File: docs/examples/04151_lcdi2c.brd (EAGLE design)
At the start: 70.6 x 33.5 mm, 14 parts, among them IC1 PCF8574T, IC2 78L05Z

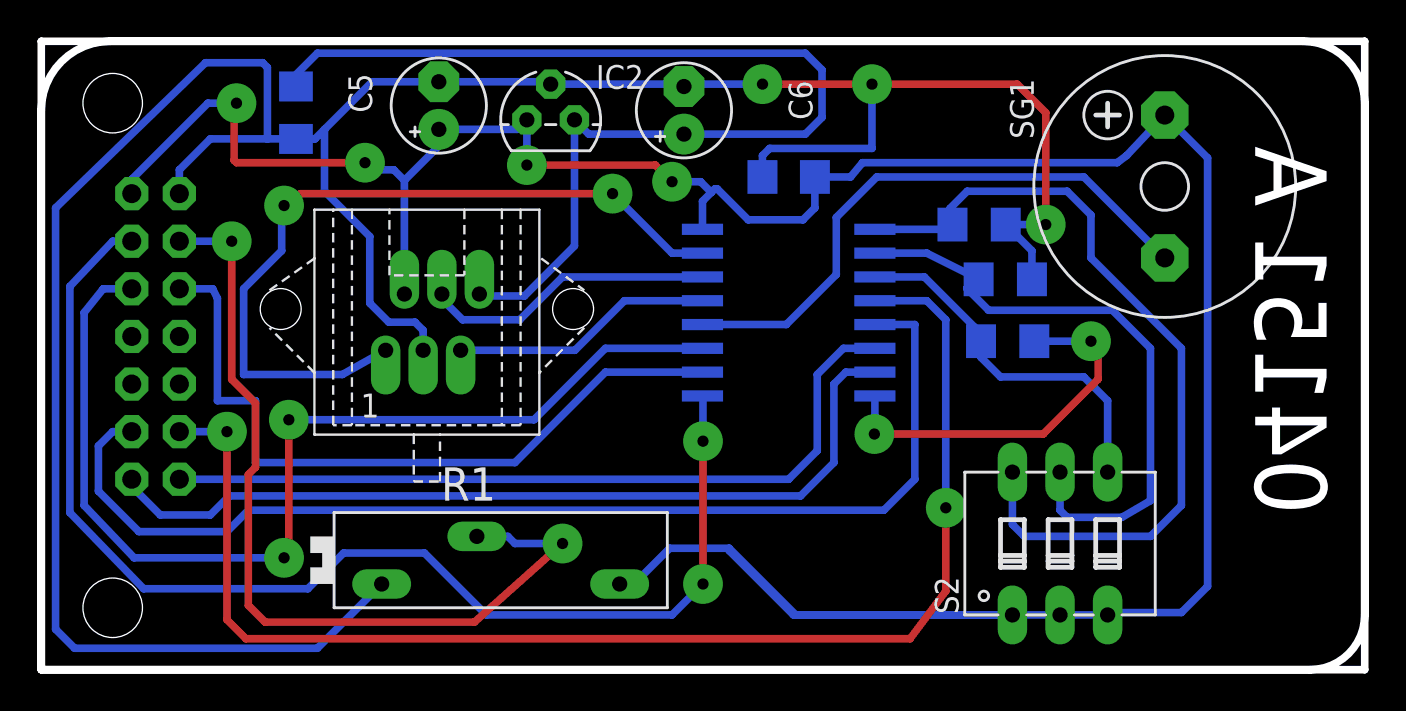
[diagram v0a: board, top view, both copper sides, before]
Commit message: Example 04151_lcdi2c.brd now include an arc at the origin, just for completeness of testing. Also updated camotics files.
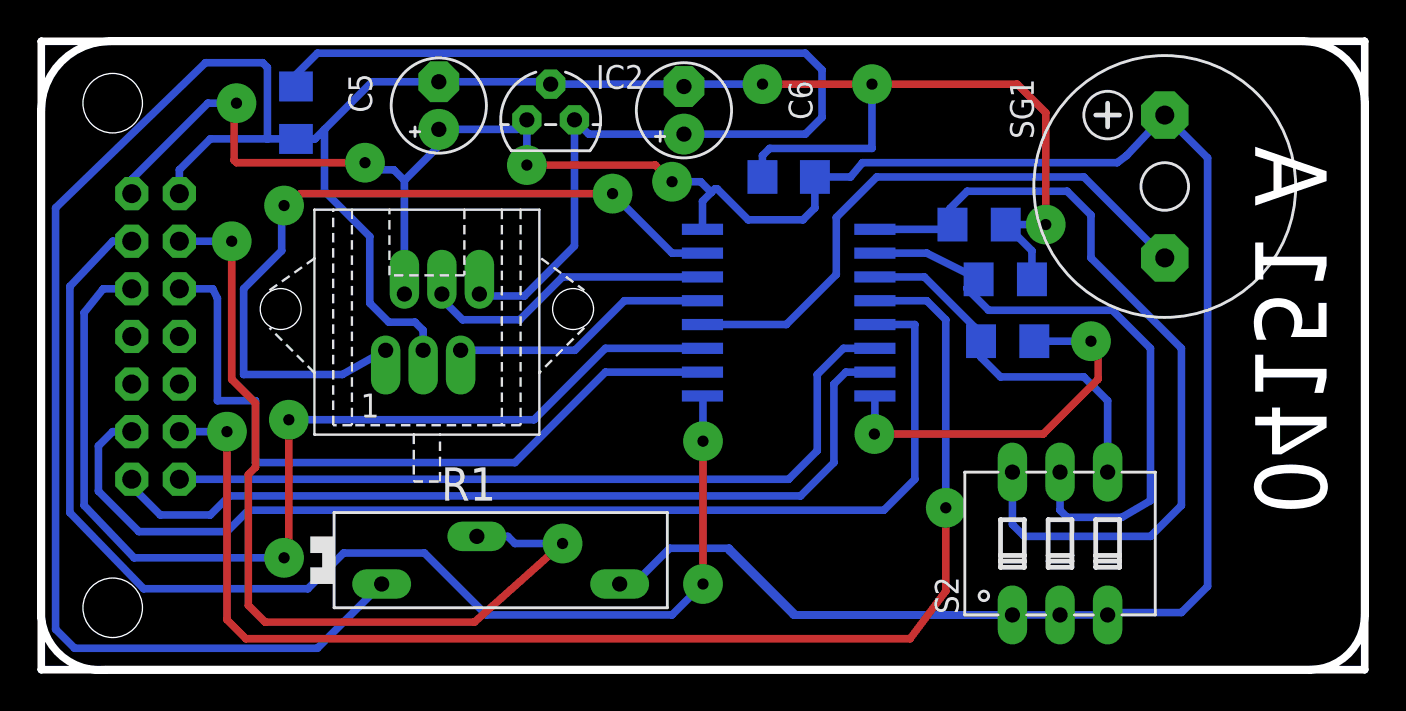
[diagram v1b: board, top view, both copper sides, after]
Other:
- outline, holes or cut-outs redrawn
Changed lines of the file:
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@@
 <?xml version="1.0" encoding="utf-8"?>
 <!DOCTYPE eagle SYSTEM "eagle.dtd">
-<eagle version="6.3">
+<eagle version="9.6.2">
 <drawing>
 <settings>
 <setting alwaysvectorfont="no"/>
+<setting keepoldvectorfont="yes"/>
 <setting verticaltext="up"/>
 </settings>
-<grid distance="0.005" unitdist="inch" unit="inch" style="lines" multiple="1" display="no" altdistance="0.025" altunitdist="inch" altunit="inch"/>
+<grid distance="0.025" unitdist="inch" unit="inch" style="lines" multiple="1" display="yes" altdistance="0.025" altunitdist="inch" altunit="inch"/>
 <layers>
 <layer number="1" name="Top" color="4" fill="1" visible="yes" active="yes"/>
@@
 <hole x="3.81" y="30.226" drill="3.175"/>
 <hole x="3.81" y="3.302" drill="3.175"/>
-<wire x1="0" y1="0" x2="0" y2="29.845" width="0.4064" layer="46"/>
+<wire x1="0" y1="2.794" x2="0" y2="29.845" width="0.4064" layer="46"/>
 <wire x1="0" y1="29.845" x2="3.683" y2="33.528" width="0.4064" layer="46" curve="-90"/>
 <wire x1="3.683" y1="33.528" x2="67.31" y2="33.528" width="0.4064" layer="46"/>
@@
 <wire x1="70.612" y1="30.226" x2="70.612" y2="2.921" width="0.4064" layer="46"/>
 <wire x1="70.612" y1="2.921" x2="67.691" y2="0" width="0.4064" layer="46" curve="-90"/>
-<wire x1="67.691" y1="0" x2="0" y2="0" width="0.4064" layer="46"/>
+<wire x1="67.691" y1="0" x2="3.429" y2="0" width="0.4064" layer="46"/>
+<wire x1="3.429" y1="0" x2="0" y2="2.794" width="0.4064" layer="46" curve="-90"/>
 </plain>
 <attributes>
@@
 <param name="dpMaxLengthDifference" value="10mm"/>
 <param name="dpGapFactor" value="2.5"/>
-<param name="checkGrid" value="0"/>
 <param name="checkAngle" value="0"/>
 <param name="checkFont" value="1"/>
 <param name="checkRestrict" value="1"/>
+<param name="checkStop" value="0"/>
+<param name="checkValues" value="0"/>
+<param name="checkNames" value="1"/>
+<param name="checkWireStubs" value="1"/>
+<param name="checkPolygonWidth" value="0"/>
 <param name="useDiameter" value="13"/>
 <param name="maxErrors" value="50"/>
@@
 <pass name="Default">
 <param name="RoutingGrid" value="10mil"/>
+<param name="AutoGrid" value="1"/>
+<param name="Efforts" value="0"/>
+<param name="TopRouterVariant" value="1"/>
 <param name="tpViaShape" value="round"/>
 <param name="PrefDir.1" value="0"/>
@@
 </autorouter>
 <elements>
-<element name="U$1" library="con-rj" package="RJ-12" value="RJ-12" x="20.574" y="18.542" rot="R180"/>
-<element name="IC1" library="micro-philips" package="SO16W" value="PCF8574T" x="39.878" y="19.05" rot="MR270"/>
-<element name="U$2" library="con-lstb" package="MA07-2" value="MA07-2-SGL" x="6.096" y="17.78" rot="MR270"/>
-<element name="R1" library="pot" package="PT-SPIN" value="" x="24.511" y="5.842"/>
-<element name="S2" library="switch-dil" package="DIP03YL" value="" x="54.356" y="6.731"/>
-<element name="R2" library="rcl" package="R1206" value="" x="51.562" y="17.526" rot="MR0"/>
-<element name="R3" library="rcl" package="R1206" value="" x="51.435" y="20.828" rot="MR0"/>
-<element name="R4" library="rcl" package="R1206" value="" x="50.038" y="23.749" rot="MR0"/>
-<element name="C1" library="rcl" package="C1206" value="100nf" x="39.878" y="26.289" rot="MR0"/>
-<element name="SG1" library="buzzer" package="F/CM12P" value="F/CM12P" x="59.944" y="25.781" rot="R90"/>
-<element name="C4" library="rcl" package="C1206" value="100nf" x="13.589" y="29.718" rot="MR270"/>
-<element name="IC2" library="linear" package="TO92" value="78L05Z" x="27.178" y="29.337"/>
+<element name="U$1" library="con-rj" package="RJ-12" value="RJ-12" x="20.574" y="18.542" smashed="yes" rot="R180"/>
+<element name="IC1" library="micro-philips" package="SO16W" value="PCF8574T" x="39.878" y="19.05" smashed="yes" rot="MR270">
+<attribute name="NAME" x="43.561" y="24.638" size="1.27" layer="26" rot="MR0"/>
+<attribute name="VALUE" x="43.561" y="12.192" size="1.27" layer="28" rot="MR0"/>
+</element>
+<element name="U$2" library="con-lstb" package="MA07-2" value="MA07-2-SGL" x="6.096" y="17.78" smashed="yes" rot="MR270">
+<attribute name="NAME" x="3.175" y="26.67" size="1.27" layer="26" ratio="10" rot="MR270"/>
+<attribute name="VALUE" x="10.287" y="20.32" size="1.27" layer="28" ratio="10" rot="MR270"/>
+</element>
+<element name="R1" library="pot" package="PT-SPIN" value="" x="24.511" y="5.842" smashed="yes">
+<attribute name="NAME" x="21.336" y="9.017" size="1.778" layer="25" ratio="10"/>
+<attribute name="VALUE" x="19.431" y="4.064" size="1.778" layer="27" ratio="10"/>
+</element>
+<element name="S2" library="switch-dil" package="DIP03YL" value="" x="54.356" y="6.731" smashed="yes">
+<attribute name="NAME" x="48.9458" y="2.9718" size="1.27" layer="25" ratio="10" rot="R90"/>
+<attribute name="VALUE" x="59.1312" y="3.5814" size="1.27" layer="27" ratio="10" rot="R90"/>
+</element>
+<element name="R2" library="rcl" package="R1206" value="" x="51.562" y="17.526" smashed="yes" rot="MR0">
+<attribute name="NAME" x="52.959" y="18.669" size="1.27" layer="26" rot="MR0"/>
+<attribute name="VALUE" x="52.959" y="15.113" size="1.27" layer="28" rot="MR0"/>
+</element>
+<element name="R3" library="rcl" package="R1206" value="" x="51.435" y="20.828" smashed="yes" rot="MR0">
+<attribute name="NAME" x="52.832" y="21.971" size="1.27" layer="26" rot="MR0"/>
+<attribute name="VALUE" x="52.832" y="18.415" size="1.27" layer="28" rot="MR0"/>
+</element>
+<element name="R4" library="rcl" package="R1206" value="" x="50.038" y="23.749" smashed="yes" rot="MR0">
+<attribute name="NAME" x="51.435" y="24.892" size="1.27" layer="26" rot="MR0"/>
+<attribute name="VALUE" x="51.435" y="21.336" size="1.27" layer="28" rot="MR0"/>
+</element>
+<element name="C1" library="rcl" package="C1206" value="100nf" x="39.878" y="26.289" smashed="yes" rot="MR0">
+<attribute name="NAME" x="41.148" y="27.432" size="1.27" layer="26" rot="MR0"/>
+<attribute name="VALUE" x="41.148" y="23.876" size="1.27" layer="28" rot="MR0"/>
+</element>
+<element name="SG1" library="buzzer" package="F/CM12P" value="F/CM12P" x="59.944" y="25.781" smashed="yes" rot="R90">
+<attribute name="NAME" x="52.959" y="28.321" size="1.27" layer="25" ratio="10" rot="R90"/>
+<attribute name="VALUE" x="63.754" y="21.336" size="1.27" layer="27" ratio="10" rot="R90"/>
+</element>
+<element name="C4" library="rcl" package="C1206" value="100nf" x="13.589" y="29.718" smashed="yes" rot="MR270">
+<attribute name="NAME" x="12.446" y="30.988" size="1.27" layer="26" rot="MR270"/>
+<attribute name="VALUE" x="16.002" y="30.988" size="1.27" layer="28" rot="MR270"/>
+</element>
+<element name="IC2" library="linear" package="TO92" value="78L05Z" x="27.178" y="29.337" smashed="yes">
+<attribute name="NAME" x="29.591" y="30.988" size="1.27" layer="25" ratio="10"/>
+<attribute name="VALUE" x="30.099" y="28.067" size="1.27" layer="27" ratio="10"/>
+</element>
 <element name="C5" library="rcl" package="!FAT_E2,5-5" value="" x="21.209" y="30.099" smashed="yes" rot="R90">
 <attribute name="NAME" x="17.653" y="29.718" size="1.27" layer="25" ratio="10" rot="R90"/>
@@
 <wire x1="14.732" y1="1.143" x2="18.161" y2="4.572" width="0.4064" layer="16"/>
 <polygon width="0.3048" layer="1" isolate="0.5334" orphans="yes" rank="6">
+<vertex x="0" y="33.528"/>
 <vertex x="0" y="0"/>
 <vertex x="70.612" y="0"/>
 <vertex x="70.612" y="33.528"/>
-<vertex x="0" y="33.528"/>
 </polygon>
+<wire x1="52.857" y1="20.828" x2="52.984" y2="17.526" width="0" layer="19" extent="16-16"/>
 </signal>
 <signal name="VCC">
@@
 </signal>
 </signals>
+<mfgpreviewcolors>
+<mfgpreviewcolor name="soldermaskcolor" color="0xC8008000"/>
+<mfgpreviewcolor name="silkscreencolor" color="0xFFFEFEFE"/>
+<mfgpreviewcolor name="backgroundcolor" color="0xFF282828"/>
+<mfgpreviewcolor name="coppercolor" color="0xFFFFBF00"/>
+<mfgpreviewcolor name="substratecolor" color="0xFF786E46"/>
+</mfgpreviewcolors>
 </board>
 </drawing>

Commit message: And everything here should be back to v3.6.5.
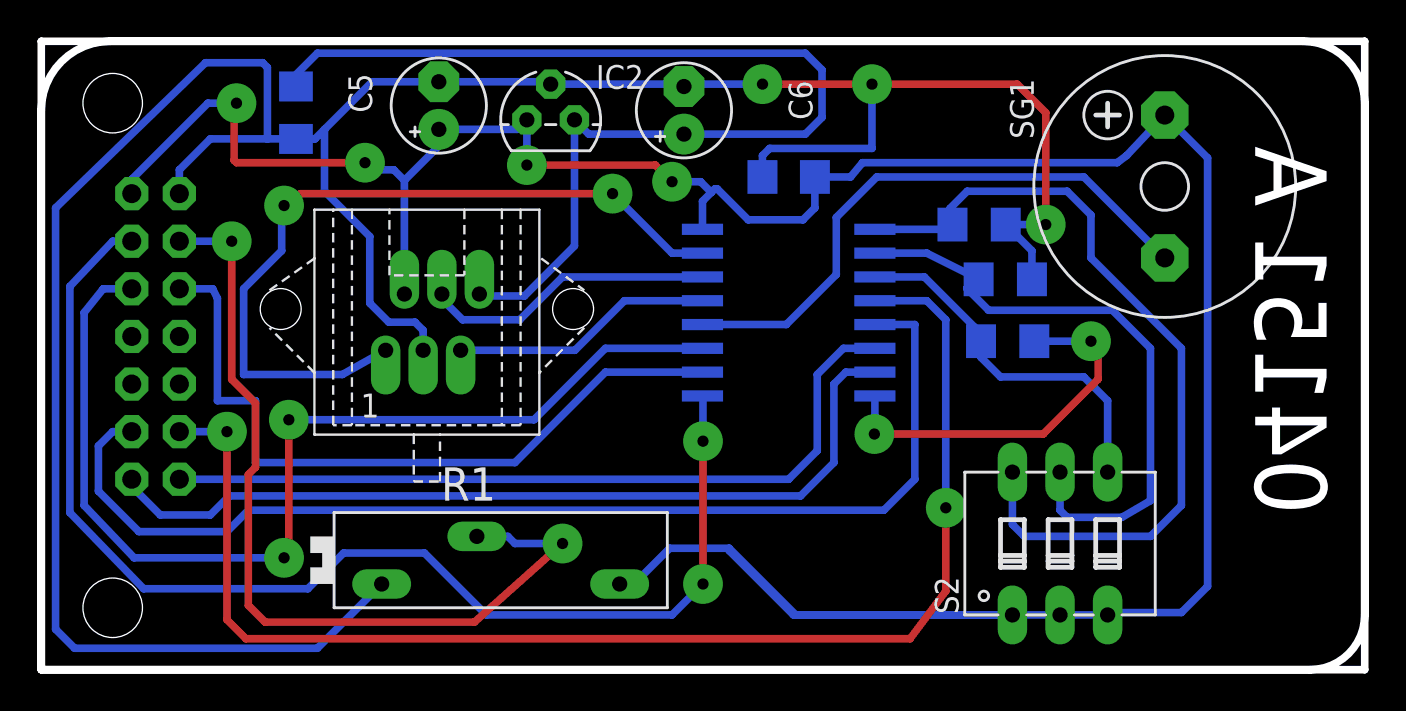
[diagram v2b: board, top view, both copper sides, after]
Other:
- outline, holes or cut-outs redrawn
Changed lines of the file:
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@@
 <?xml version="1.0" encoding="utf-8"?>
 <!DOCTYPE eagle SYSTEM "eagle.dtd">
-<eagle version="9.6.2">
+<eagle version="6.3">
 <drawing>
 <settings>
 <setting alwaysvectorfont="no"/>
-<setting keepoldvectorfont="yes"/>
 <setting verticaltext="up"/>
 </settings>
-<grid distance="0.025" unitdist="inch" unit="inch" style="lines" multiple="1" display="yes" altdistance="0.025" altunitdist="inch" altunit="inch"/>
+<grid distance="0.005" unitdist="inch" unit="inch" style="lines" multiple="1" display="no" altdistance="0.025" altunitdist="inch" altunit="inch"/>
 <layers>
 <layer number="1" name="Top" color="4" fill="1" visible="yes" active="yes"/>
@@
 <hole x="3.81" y="30.226" drill="3.175"/>
 <hole x="3.81" y="3.302" drill="3.175"/>
-<wire x1="0" y1="2.794" x2="0" y2="29.845" width="0.4064" layer="46"/>
+<wire x1="0" y1="0" x2="0" y2="29.845" width="0.4064" layer="46"/>
 <wire x1="0" y1="29.845" x2="3.683" y2="33.528" width="0.4064" layer="46" curve="-90"/>
 <wire x1="3.683" y1="33.528" x2="67.31" y2="33.528" width="0.4064" layer="46"/>
@@
 <wire x1="70.612" y1="30.226" x2="70.612" y2="2.921" width="0.4064" layer="46"/>
 <wire x1="70.612" y1="2.921" x2="67.691" y2="0" width="0.4064" layer="46" curve="-90"/>
-<wire x1="67.691" y1="0" x2="3.429" y2="0" width="0.4064" layer="46"/>
-<wire x1="3.429" y1="0" x2="0" y2="2.794" width="0.4064" layer="46" curve="-90"/>
+<wire x1="67.691" y1="0" x2="0" y2="0" width="0.4064" layer="46"/>
 </plain>
 <attributes>
@@
 <param name="dpMaxLengthDifference" value="10mm"/>
 <param name="dpGapFactor" value="2.5"/>
+<param name="checkGrid" value="0"/>
 <param name="checkAngle" value="0"/>
 <param name="checkFont" value="1"/>
 <param name="checkRestrict" value="1"/>
-<param name="checkStop" value="0"/>
-<param name="checkValues" value="0"/>
-<param name="checkNames" value="1"/>
-<param name="checkWireStubs" value="1"/>
-<param name="checkPolygonWidth" value="0"/>
 <param name="useDiameter" value="13"/>
 <param name="maxErrors" value="50"/>
@@
 <pass name="Default">
 <param name="RoutingGrid" value="10mil"/>
-<param name="AutoGrid" value="1"/>
-<param name="Efforts" value="0"/>
-<param name="TopRouterVariant" value="1"/>
 <param name="tpViaShape" value="round"/>
 <param name="PrefDir.1" value="0"/>
@@
 </autorouter>
 <elements>
-<element name="U$1" library="con-rj" package="RJ-12" value="RJ-12" x="20.574" y="18.542" smashed="yes" rot="R180"/>
-<element name="IC1" library="micro-philips" package="SO16W" value="PCF8574T" x="39.878" y="19.05" smashed="yes" rot="MR270">
-<attribute name="NAME" x="43.561" y="24.638" size="1.27" layer="26" rot="MR0"/>
-<attribute name="VALUE" x="43.561" y="12.192" size="1.27" layer="28" rot="MR0"/>
-</element>
-<element name="U$2" library="con-lstb" package="MA07-2" value="MA07-2-SGL" x="6.096" y="17.78" smashed="yes" rot="MR270">
-<attribute name="NAME" x="3.175" y="26.67" size="1.27" layer="26" ratio="10" rot="MR270"/>
-<attribute name="VALUE" x="10.287" y="20.32" size="1.27" layer="28" ratio="10" rot="MR270"/>
-</element>
-<element name="R1" library="pot" package="PT-SPIN" value="" x="24.511" y="5.842" smashed="yes">
-<attribute name="NAME" x="21.336" y="9.017" size="1.778" layer="25" ratio="10"/>
-<attribute name="VALUE" x="19.431" y="4.064" size="1.778" layer="27" ratio="10"/>
-</element>
-<element name="S2" library="switch-dil" package="DIP03YL" value="" x="54.356" y="6.731" smashed="yes">
-<attribute name="NAME" x="48.9458" y="2.9718" size="1.27" layer="25" ratio="10" rot="R90"/>
-<attribute name="VALUE" x="59.1312" y="3.5814" size="1.27" layer="27" ratio="10" rot="R90"/>
-</element>
-<element name="R2" library="rcl" package="R1206" value="" x="51.562" y="17.526" smashed="yes" rot="MR0">
-<attribute name="NAME" x="52.959" y="18.669" size="1.27" layer="26" rot="MR0"/>
-<attribute name="VALUE" x="52.959" y="15.113" size="1.27" layer="28" rot="MR0"/>
-</element>
-<element name="R3" library="rcl" package="R1206" value="" x="51.435" y="20.828" smashed="yes" rot="MR0">
-<attribute name="NAME" x="52.832" y="21.971" size="1.27" layer="26" rot="MR0"/>
-<attribute name="VALUE" x="52.832" y="18.415" size="1.27" layer="28" rot="MR0"/>
-</element>
-<element name="R4" library="rcl" package="R1206" value="" x="50.038" y="23.749" smashed="yes" rot="MR0">
-<attribute name="NAME" x="51.435" y="24.892" size="1.27" layer="26" rot="MR0"/>
-<attribute name="VALUE" x="51.435" y="21.336" size="1.27" layer="28" rot="MR0"/>
-</element>
-<element name="C1" library="rcl" package="C1206" value="100nf" x="39.878" y="26.289" smashed="yes" rot="MR0">
-<attribute name="NAME" x="41.148" y="27.432" size="1.27" layer="26" rot="MR0"/>
-<attribute name="VALUE" x="41.148" y="23.876" size="1.27" layer="28" rot="MR0"/>
-</element>
-<element name="SG1" library="buzzer" package="F/CM12P" value="F/CM12P" x="59.944" y="25.781" smashed="yes" rot="R90">
-<attribute name="NAME" x="52.959" y="28.321" size="1.27" layer="25" ratio="10" rot="R90"/>
-<attribute name="VALUE" x="63.754" y="21.336" size="1.27" layer="27" ratio="10" rot="R90"/>
-</element>
-<element name="C4" library="rcl" package="C1206" value="100nf" x="13.589" y="29.718" smashed="yes" rot="MR270">
-<attribute name="NAME" x="12.446" y="30.988" size="1.27" layer="26" rot="MR270"/>
-<attribute name="VALUE" x="16.002" y="30.988" size="1.27" layer="28" rot="MR270"/>
-</element>
-<element name="IC2" library="linear" package="TO92" value="78L05Z" x="27.178" y="29.337" smashed="yes">
-<attribute name="NAME" x="29.591" y="30.988" size="1.27" layer="25" ratio="10"/>
-<attribute name="VALUE" x="30.099" y="28.067" size="1.27" layer="27" ratio="10"/>
-</element>
+<element name="U$1" library="con-rj" package="RJ-12" value="RJ-12" x="20.574" y="18.542" rot="R180"/>
+<element name="IC1" library="micro-philips" package="SO16W" value="PCF8574T" x="39.878" y="19.05" rot="MR270"/>
+<element name="U$2" library="con-lstb" package="MA07-2" value="MA07-2-SGL" x="6.096" y="17.78" rot="MR270"/>
+<element name="R1" library="pot" package="PT-SPIN" value="" x="24.511" y="5.842"/>
+<element name="S2" library="switch-dil" package="DIP03YL" value="" x="54.356" y="6.731"/>
+<element name="R2" library="rcl" package="R1206" value="" x="51.562" y="17.526" rot="MR0"/>
+<element name="R3" library="rcl" package="R1206" value="" x="51.435" y="20.828" rot="MR0"/>
+<element name="R4" library="rcl" package="R1206" value="" x="50.038" y="23.749" rot="MR0"/>
+<element name="C1" library="rcl" package="C1206" value="100nf" x="39.878" y="26.289" rot="MR0"/>
+<element name="SG1" library="buzzer" package="F/CM12P" value="F/CM12P" x="59.944" y="25.781" rot="R90"/>
+<element name="C4" library="rcl" package="C1206" value="100nf" x="13.589" y="29.718" rot="MR270"/>
+<element name="IC2" library="linear" package="TO92" value="78L05Z" x="27.178" y="29.337"/>
 <element name="C5" library="rcl" package="!FAT_E2,5-5" value="" x="21.209" y="30.099" smashed="yes" rot="R90">
 <attribute name="NAME" x="17.653" y="29.718" size="1.27" layer="25" ratio="10" rot="R90"/>
@@
 <wire x1="14.732" y1="1.143" x2="18.161" y2="4.572" width="0.4064" layer="16"/>
 <polygon width="0.3048" layer="1" isolate="0.5334" orphans="yes" rank="6">
-<vertex x="0" y="33.528"/>
 <vertex x="0" y="0"/>
 <vertex x="70.612" y="0"/>
 <vertex x="70.612" y="33.528"/>
+<vertex x="0" y="33.528"/>
 </polygon>
-<wire x1="52.857" y1="20.828" x2="52.984" y2="17.526" width="0" layer="19" extent="16-16"/>
 </signal>
 <signal name="VCC">
@@
 </signal>
 </signals>
-<mfgpreviewcolors>
-<mfgpreviewcolor name="soldermaskcolor" color="0xC8008000"/>
-<mfgpreviewcolor name="silkscreencolor" color="0xFFFEFEFE"/>
-<mfgpreviewcolor name="backgroundcolor" color="0xFF282828"/>
-<mfgpreviewcolor name="coppercolor" color="0xFFFFBF00"/>
-<mfgpreviewcolor name="substratecolor" color="0xFF786E46"/>
-</mfgpreviewcolors>
 </board>
 </drawing>
